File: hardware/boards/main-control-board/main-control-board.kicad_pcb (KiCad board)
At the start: 2 copper layers, 120 x 55 mm, 20 parts, among them J2 Conn_OLED, J7 Conn_ESP32_L, J8 Conn_ESP32_R, U1 PCA9685PW,118, U2 HX PZ2.54-3X5P ZZ

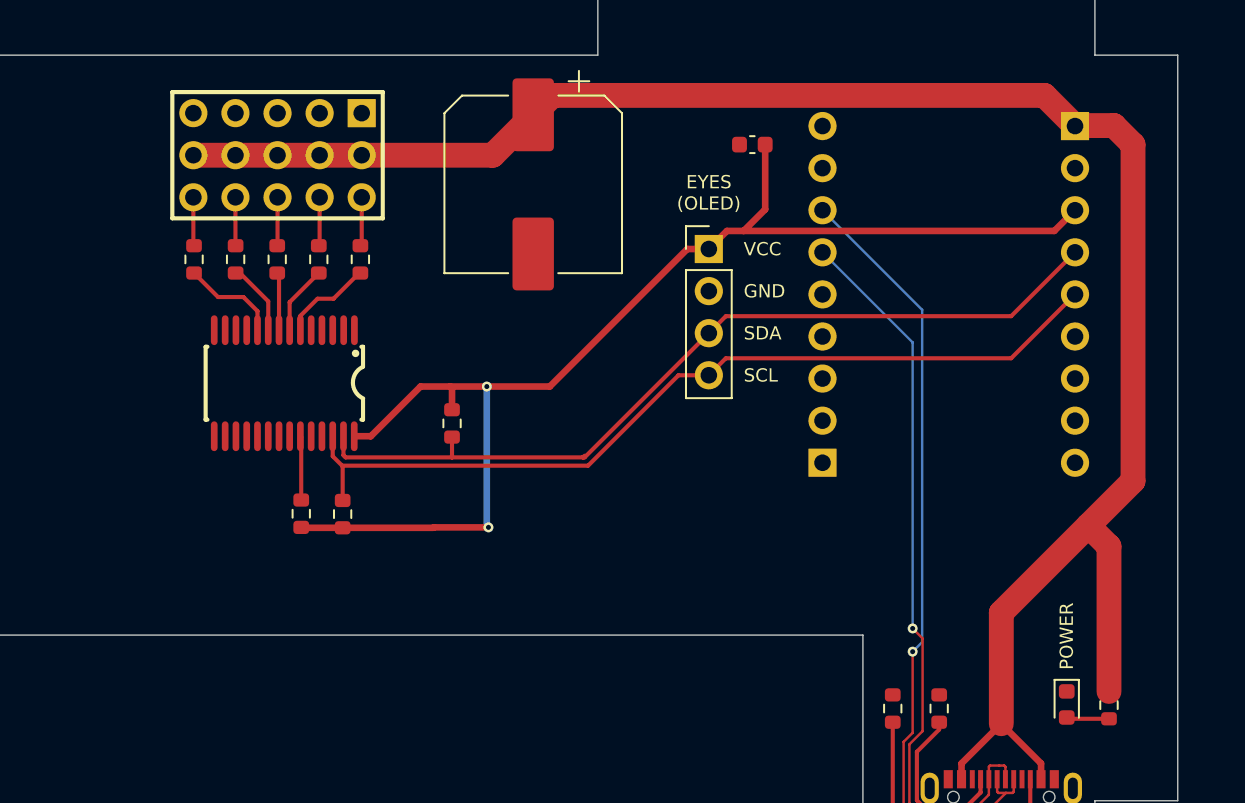
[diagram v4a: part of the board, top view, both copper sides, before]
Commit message: set FT Rotation Offset to fix JLCPCB orientation
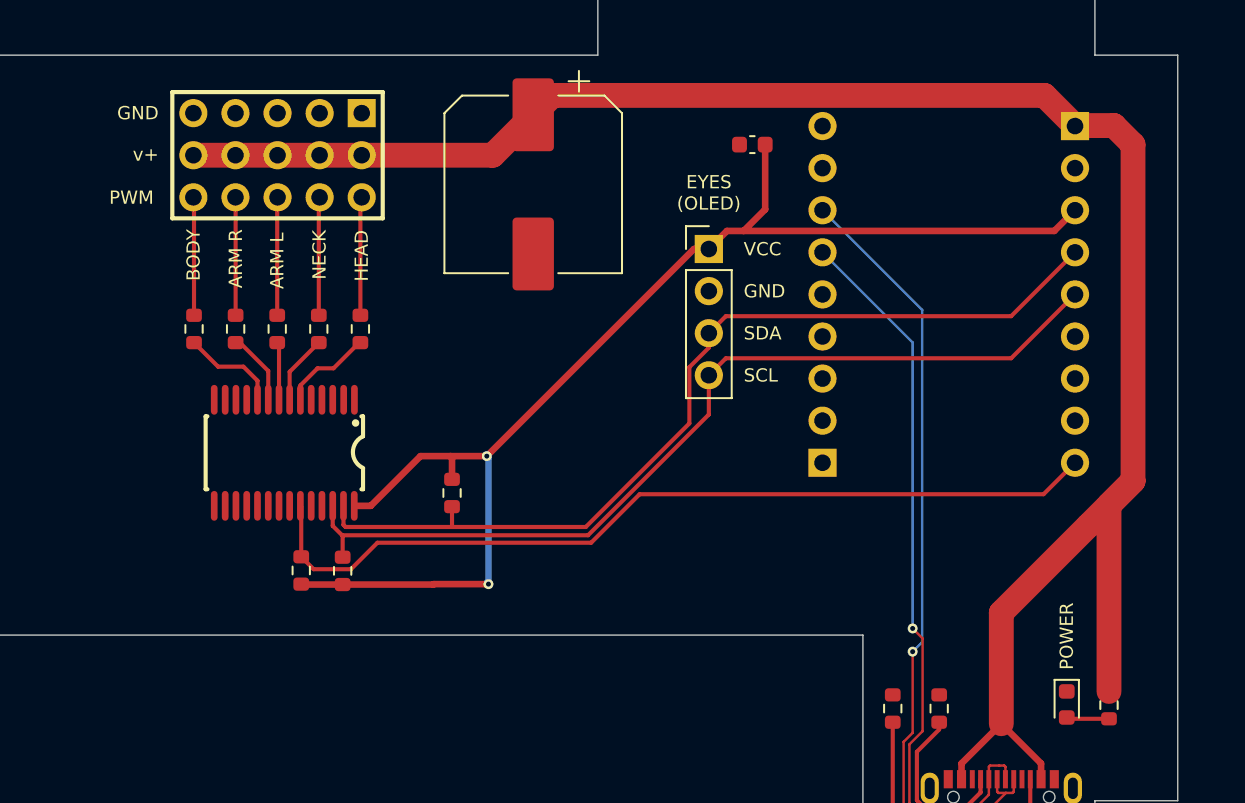
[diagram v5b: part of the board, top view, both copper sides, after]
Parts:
- moved R10 4.20 mm to (143.1, 101.5)
- moved R5 4.20 mm to (158.7, 111.4)
- moved R6 4.20 mm to (153.2, 101.5)
- moved R7 4.20 mm to (150.7, 101.5)
- moved R8 4.20 mm to (148.2, 101.5)
- moved R9 4.20 mm to (145.6, 101.5)
- moved U1 4.20 mm to (148.6, 109.0)
- moved R3 3.42 mm to (149.6, 116.1)
- moved R4 3.42 mm to (152.1, 116.1)
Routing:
- net /ESP32/GP5: track 3.87 -> 52.8 mm
- net Net-(R6-Pad2): track 2.95 -> 7.27 mm
- net Net-(R7-Pad2): track 2.94 -> 7.21 mm
- net Net-(R10-Pad2): track 2.94 -> 7.19 mm
- net Net-(R8-Pad2): track 2.93 -> 7.16 mm
- net Net-(R9-Pad2): track 2.92 -> 7.14 mm
- net /I2C_SDA: track 51.8 -> 55.9 mm
- net +5V: track 116.9 -> 119.7 mm
- net /I2C_SCL: track 52.6 -> 55.0 mm
- net +3.3V: track 76.9 -> 78.0 mm
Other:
- board text added: "ARM L"
- board text added: "ARM R"
- board text added: "BODY"
- board text added: "HEAD"
- board text added: "NECK"
- board text added: "PWM"
- board text added: "v+"

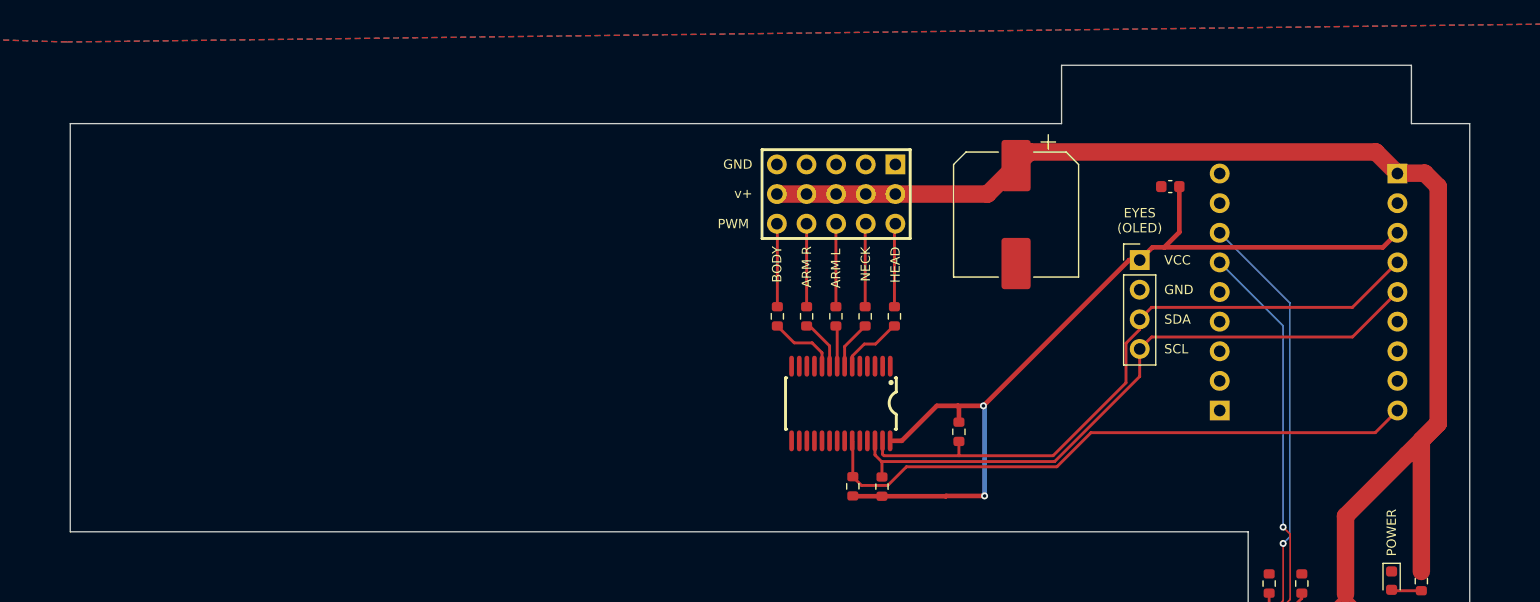
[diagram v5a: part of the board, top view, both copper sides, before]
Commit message: integrate audio module
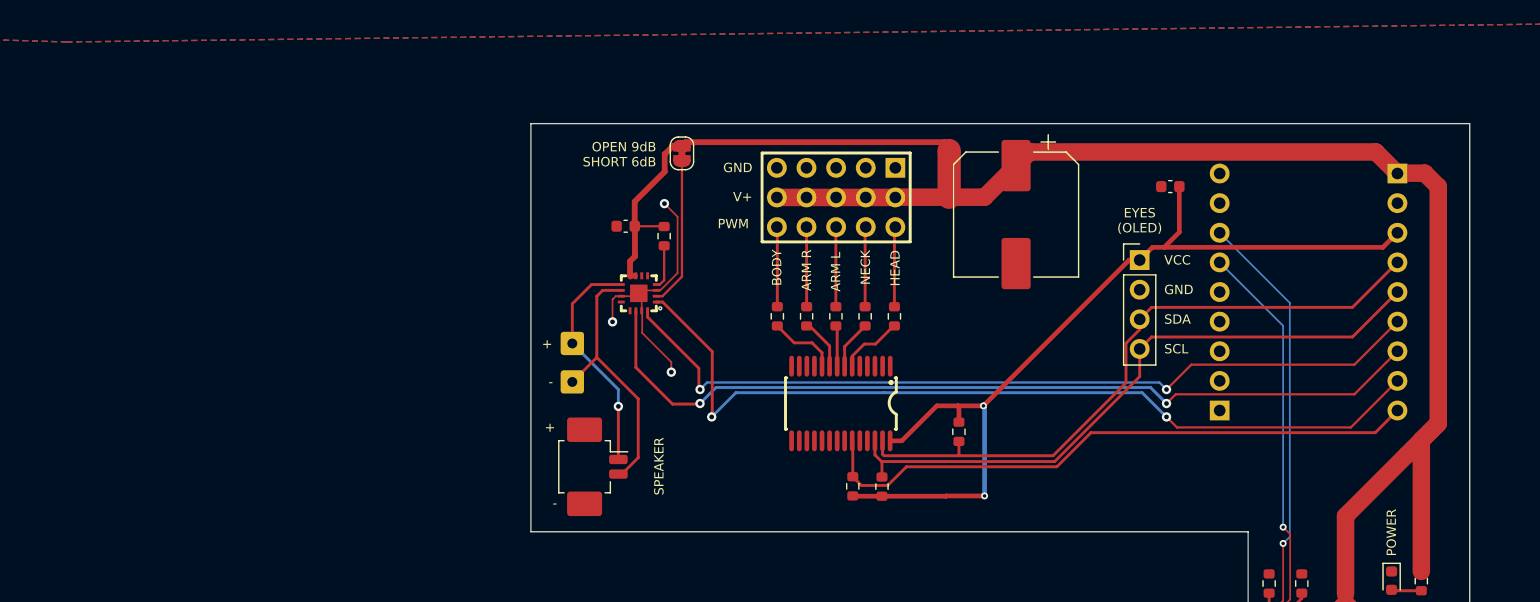
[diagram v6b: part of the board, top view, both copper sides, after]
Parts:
- added C3: 100nF, Capacitor_SMD:C_0603_1608Metric, F.Cu at (130.1, 93.8)
- added J1: Conn_01x02_Pin_Speaker, Connector_Molex:Molex_PicoBlade_53261-0271_1x02-1MP_P1.25mm_Horizontal, F.Cu at (127.1, 114.4)
- added JP1: SolderJumper_gain_6dB_limit, Jumper:SolderJumper-2_P1.3mm_Bridged_RoundedPad1.0x1.5mm, F.Cu at (134.9, 87.5)
- added NT1: NetTie_2, NetTie:NetTie-2_SMD_Pad2.0mm, F.Cu at (157.9, 89.3)
- added R12: 1M, Resistor_SMD:R_0603_1608Metric, F.Cu at (133.4, 94.7)
- added TP1: TestPoint, Connector_Wire:SolderWire-0.25sqmm_1x01_D0.65mm_OD2mm, F.Cu at (125.5, 103.8)
- added TP2: TestPoint, Connector_Wire:SolderWire-0.25sqmm_1x01_D0.65mm_OD2mm, F.Cu at (125.5, 107.2)
- added U3: MAX98357AETE+T, easyeda:TQFN-16_L3.0-W3.0-P0.50-BL-EP1.5, F.Cu at (131.2, 99.5)
- moved U2 0.29 mm to (148.2, 91.3)
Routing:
- net /I2S_DIN: track 0.00 -> 74.6 mm, vias 0 -> 2
- net /I2S_LRC: track 0.00 -> 74.3 mm, vias 0 -> 2
- net /I2S_BCLK: track 0.00 -> 71.6 mm, vias 0 -> 2
- net /Audio/AUDIO_5V: track 0.00 -> 39.8 mm
- net Net-(J1-Pin_2): track 0.00 -> 22.9 mm
- net GND: track 0.00 -> 22.8 mm, vias 0 -> 3
- net Net-(J1-Pin_1): track 0.00 -> 19.9 mm, vias 0 -> 1
- net Net-(JP1-B): track 0.00 -> 12.8 mm
- net Net-(U3-~{SD_MODE}): track 0.00 -> 3.78 mm
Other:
- board size 120 x 55 mm -> 80.5 x 50 mm
- board text added: "+"
- board text added: "-"
- board text added: "OPEN 9dB SHORT 6dB"
- board text added: "SPEAKER"
- board text added: "V+"
- board text removed: "v+"

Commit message: improve board visuals
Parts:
- added ?: , , F.Cu at (137.0, 116.5)
- added REF**: MountingHole_2.2mm_M2, MountingHole:MountingHole_2.2mm_M2, F.Cu at (125.5, 93.5)
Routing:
- net +3.3V: track 78.0 -> 83.0 mm
- net GND: vias 3 -> 30
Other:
- outline, holes or cut-outs redrawn
- board text added: "TINY SOFTWARE ENGINEER Main Control Board REV #2 | 2026-09-25 github.com/jamro/tiny-engineer"
- board text removed: "Main Control Board REV #2 | 2026-09-22 github.com/jamro/tiny-engineer"
- board text removed: "TINY SOFTWARE ENGINEER"

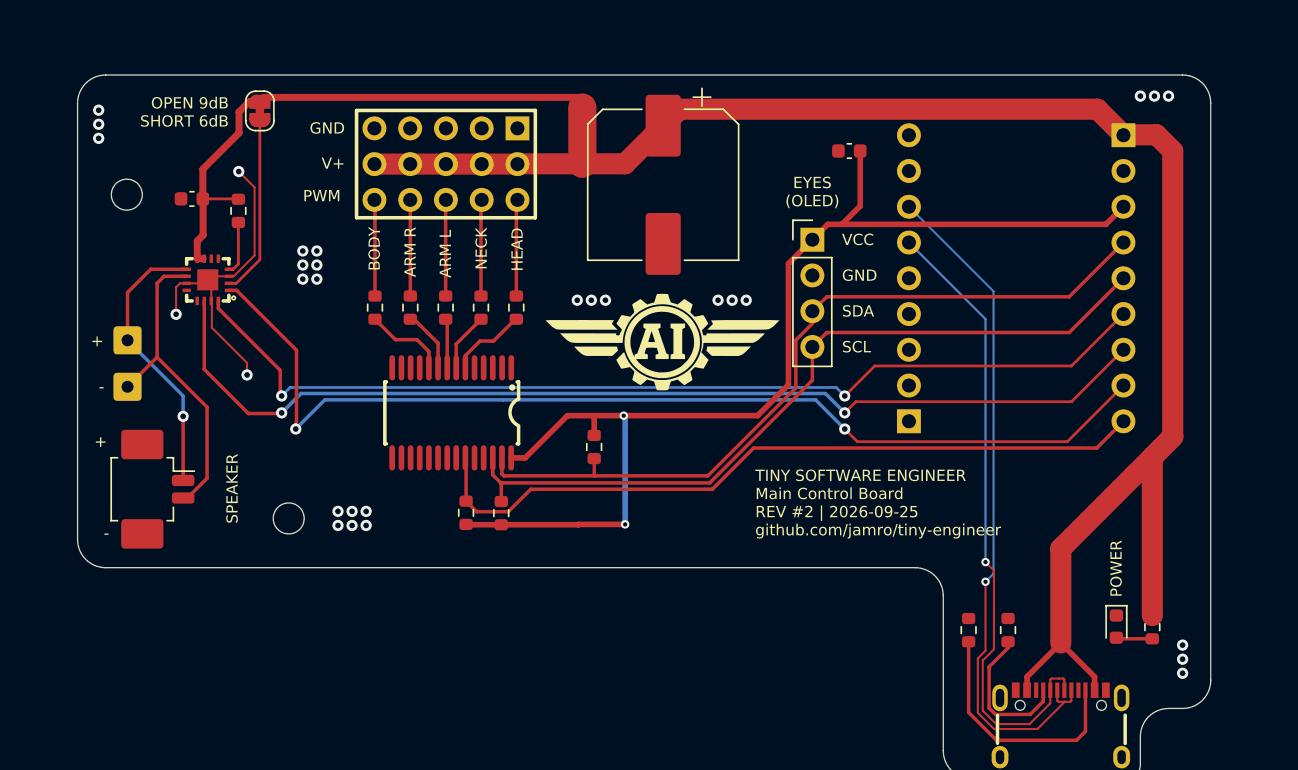
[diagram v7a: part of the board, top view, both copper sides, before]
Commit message: add I2C extension port
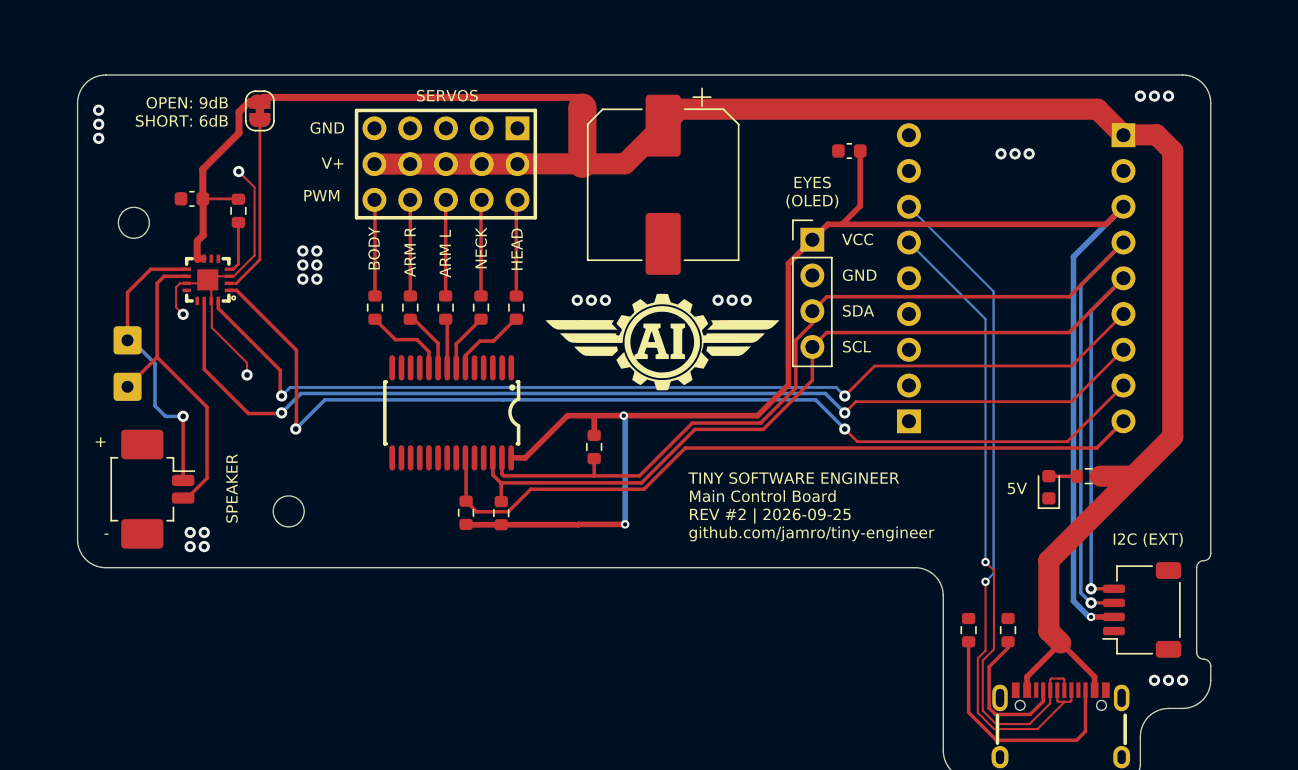
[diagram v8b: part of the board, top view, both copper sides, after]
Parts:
- removed ?: , 
- removed REF**: MountingHole_2.2mm_M2, MountingHole:MountingHole_2.2mm_M2
- added H1: MountingHole, MountingHole:MountingHole_2.2mm_M2, F.Cu at (126.0, 95.5)
- added H2: MountingHole, MountingHole:MountingHole_2.2mm_M2, F.Cu at (137.0, 116.0)
- added J3: Conn_extension, Connector_JST:JST_SH_SM04B-SRSS-TB_1x04-1MP_P1.00mm_Horizontal, F.Cu at (197.6, 123.0)
- moved R11 11.6 mm to (193.8, 113.5), turned to 180 degrees
- moved D1 11.0 mm to (191.0, 114.3), turned to 90 degrees
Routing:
- net +3.3V: track 83.0 -> 115.9 mm, vias 2 -> 3
- net /I2C_SDA: track 55.9 -> 84.7 mm, vias 0 -> 1
- net /I2C_SCL: track 55.0 -> 79.6 mm, vias 0 -> 1
- net +5V: track 119.9 -> 109.6 mm
- net Net-(J1-Pin_1): track 19.9 -> 20.8 mm
- net Net-(D1-A): track 2.58 -> 2.00 mm
- net GND: track 22.8 -> 23.0 mm, vias 30 -> 31
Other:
- outline, holes or cut-outs redrawn
- board text added: "DO NOT USE ESP USB WHILE BOARD USB IS CONNECTED!"
- board text added: "I2C (EXT)"
- board text added: "OPEN: 9dB SHORT: 6dB"
- board text added: "SERVOS"
- board text removed: "OPEN 9dB SHORT 6dB"
- board text removed: "POWER"
